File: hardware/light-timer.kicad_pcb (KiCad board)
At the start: 4 copper layers, 50 x 70 mm, 4 parts, among them P1 Power Connector, P2 Pushbutton Connector, P3 Relay Connector, U1 LeoStick

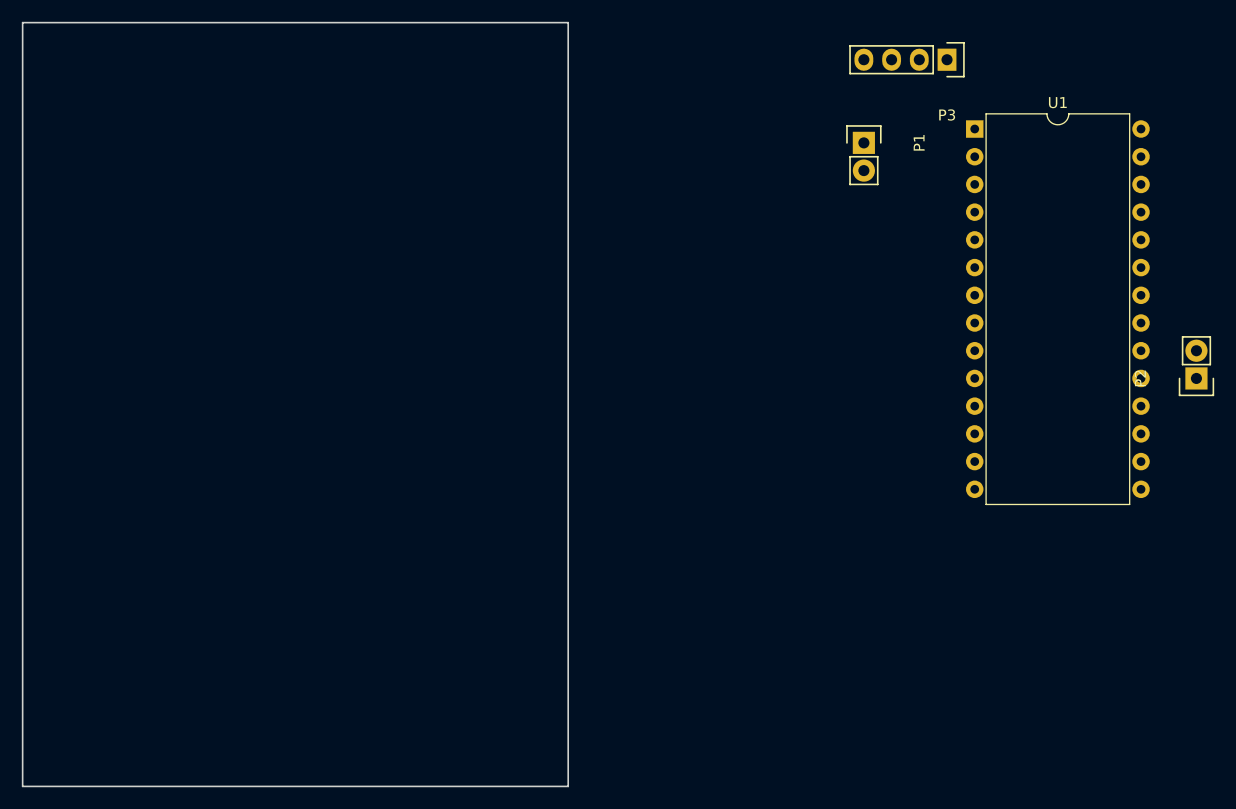
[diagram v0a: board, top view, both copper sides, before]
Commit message: Add duration DIP switches, board layout
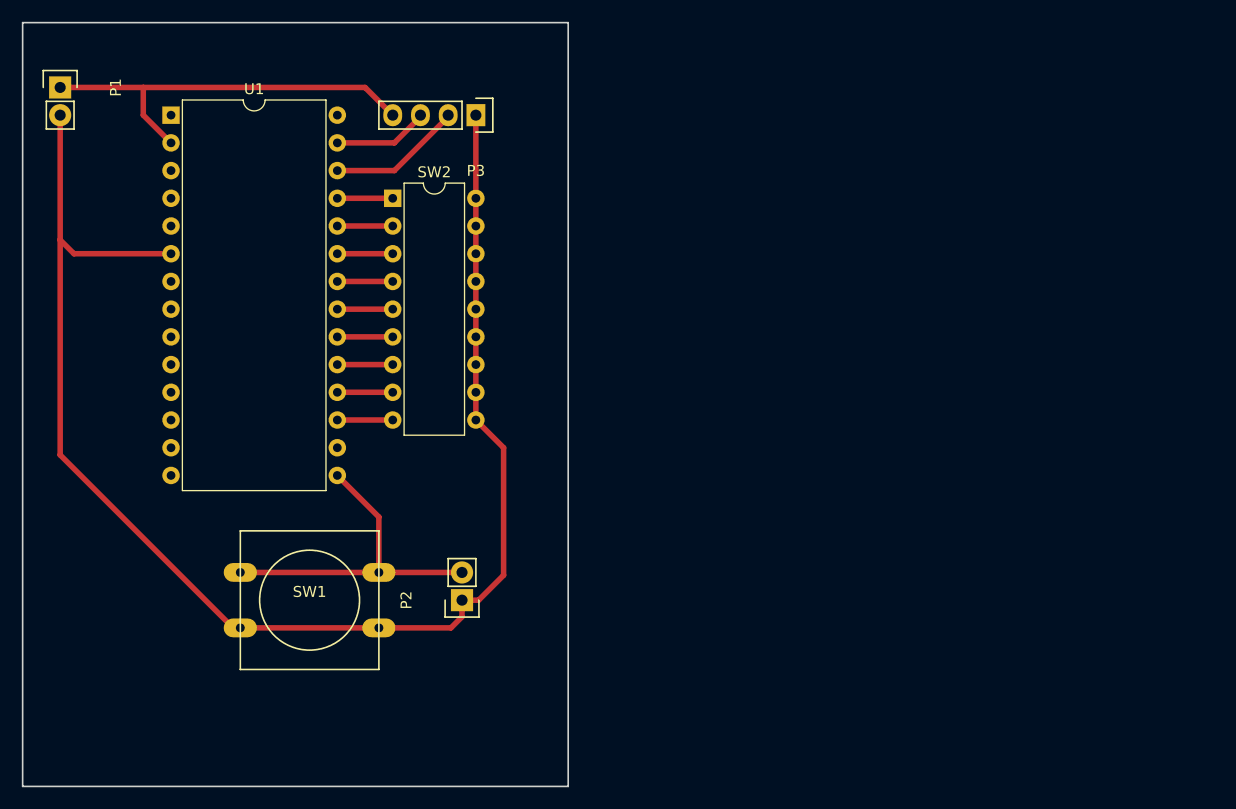
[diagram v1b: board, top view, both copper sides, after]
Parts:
- added SW1: On-board Pushbutton, Buttons_Switches_ThroughHole:SW_PUSH-12mm, F.Cu at (96.6, 123.5)
- added SW2: Duration Switches, Housings_DIP:DIP-18_W7.62mm, F.Cu at (104.2, 86.6)
- moved P1 73.8 mm to (73.7, 76.5)
- moved U1 73.7 mm to (83.9, 79.0)
- moved P2 70.3 mm to (110.5, 123.5)
- moved P3 43.5 mm to (111.8, 79.0)
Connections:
- P2 pad 1: Net-(P2-Pad1) -> GND
- P2 pad 2: GND -> Net-(P2-Pad2)
- U1 pad 15: Net-(U1-Pad15) -> Net-(P2-Pad2)
- U1 pad 17: Net-(U1-Pad17) -> /1_16HR
- U1 pad 18: Net-(U1-Pad18) -> /1_8HR
- U1 pad 19: Net-(P2-Pad1) -> /1_4HR
- U1 pad 20: Net-(U1-Pad20) -> /1_2HR
- U1 pad 21: Net-(U1-Pad21) -> /1HR
- U1 pad 22: Net-(U1-Pad22) -> /2HR
- U1 pad 23: Net-(U1-Pad23) -> /4HR
- U1 pad 24: Net-(U1-Pad24) -> /8HR
- U1 pad 25: Net-(U1-Pad25) -> /16HR
- U1 pad 26: Net-(U1-Pad26) -> /IN1
- U1 pad 27: Net-(U1-Pad27) -> /IN2
- U1 pad 28: /IN1 -> Net-(U1-Pad28)
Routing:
- net GND: track 0.00 -> 135.1 mm
- net VCC: track 0.00 -> 37.7 mm
- net Net-(P2-Pad2): track 0.00 -> 30.8 mm
- net /IN1: track 0.00 -> 12.4 mm
- net /IN2: track 0.00 -> 8.76 mm
- net /8HR: track 0.00 -> 5.08 mm
- net /4HR: track 0.00 -> 5.08 mm
- net /2HR: track 0.00 -> 5.08 mm
- net /1_8HR: track 0.00 -> 5.08 mm
- net /1_4HR: track 0.00 -> 5.08 mm
- net /1_2HR: track 0.00 -> 5.08 mm
- net /1_16HR: track 0.00 -> 5.08 mm
- net /1HR: track 0.00 -> 5.08 mm
- net /16HR: track 0.00 -> 5.08 mm
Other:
- net class Default: clearance 0.2 -> 0.254; trace_width 0.25 -> 0.508; via_dia 0.6 -> 0.635; via_drill 0.4 -> 0.381
- rule trace_clearance: 0.2 -> 0.254
